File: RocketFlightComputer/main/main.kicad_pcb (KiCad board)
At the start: 4 copper layers, 53.7 x 53.7 mm, 127 parts, among them Q1 SI2302, Q2 SI2302, Q3 SI2302, Y1 32.768kHz, Y3 32.768kHz, Y4 32.768kHz, Y5 XRCGB24M000F2P29R0

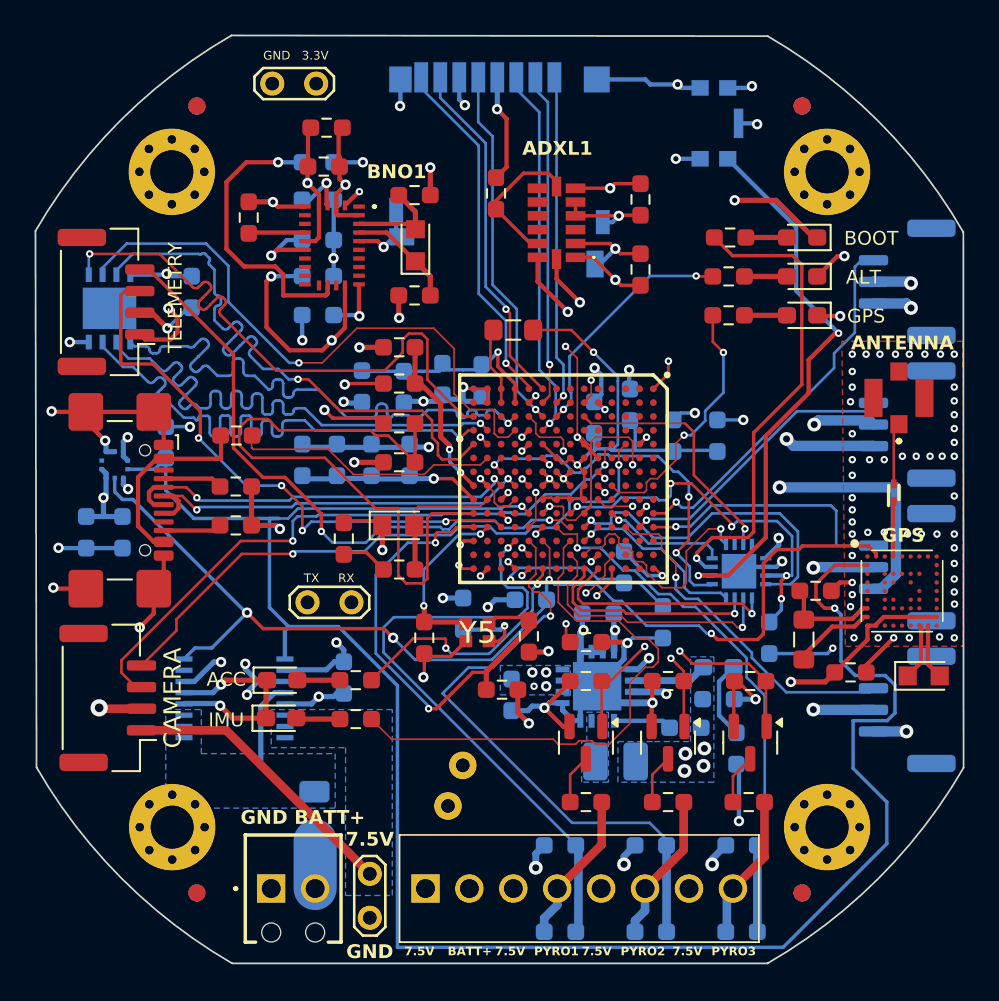
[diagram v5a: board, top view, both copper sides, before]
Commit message: Change of winbond flash to other one supported by teensy bootloader since winbond is out of stock
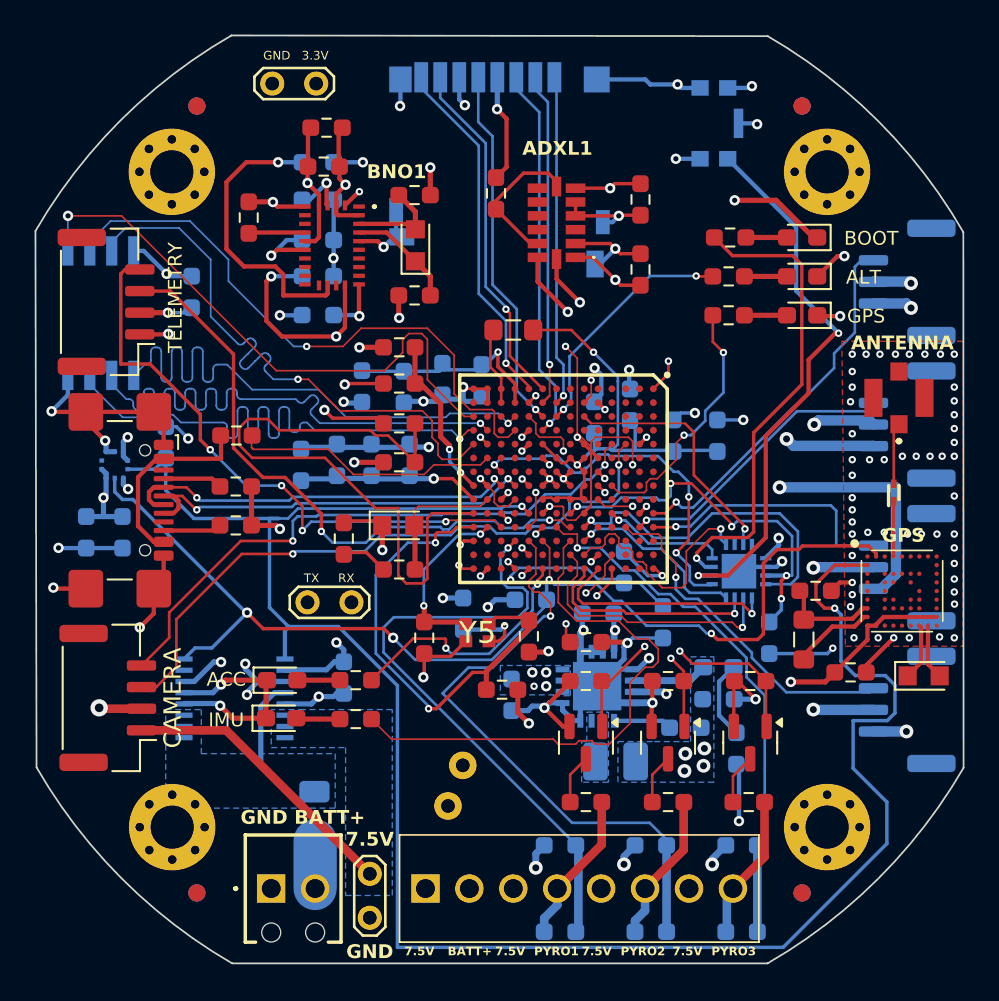
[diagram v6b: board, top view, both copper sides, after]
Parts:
- removed W25Q64JVXGIM_TR1: FLASH, footprint:SON80P400X400X50-9N
- added FLASH1: GD25Q64ESIG, footprint:GD25Q64ESIG, B.Cu at (86.8, 47.8)
- moved C6 0.30 mm to (98.4, 56.5)
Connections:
- MIMXRT1062DVL6B1 pad G11: /Xbee_RX -> /Xbee_TX
- MIMXRT1062DVL6B1 pad M11: /Xbee_TX -> /Xbee_RX
- S4B-PH-K-S_LF__SN_2 pad 3: /Cam_TX -> /Cam_RX
- S4B-PH-K-S_LF__SN_2 pad 4: /Cam_RX -> /Cam_TX
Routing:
- net GNDREF: track 255.0 -> 243.1 mm, vias 131 -> 130
- net /Cam_TX: track 37.5 -> 34.6 mm
- net +3.3V: track 111.2 -> 108.6 mm
- net /Xbee_TX: track 33.4 -> 35.9 mm, vias 4 -> 2
- net /Xbee_RX: track 36.4 -> 34.5 mm, vias 2 -> 4
- net /Cam_RX: track 35.9 -> 37.7 mm
- net /CS: track 33.3 -> 34.4 mm
- net Net-(MIMXRT1062DVL6B1-DCDC_IN_1): track 12.0 -> 11.0 mm
- net /BNO085_SCL: track 33.5 -> 32.8 mm
- net Net-(ADXL1-ADDR/SDO): track 8.37 -> 7.66 mm
- net /SD_B0_05: track 19.3 -> 18.6 mm
- net /CLK: track 34.8 -> 34.1 mm
- net /Servo4_PWM: track 21.8 -> 21.1 mm
- net /SD_B0_00: track 21.7 -> 21.0 mm
- net /SD_B0_03: track 20.6 -> 20.0 mm
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
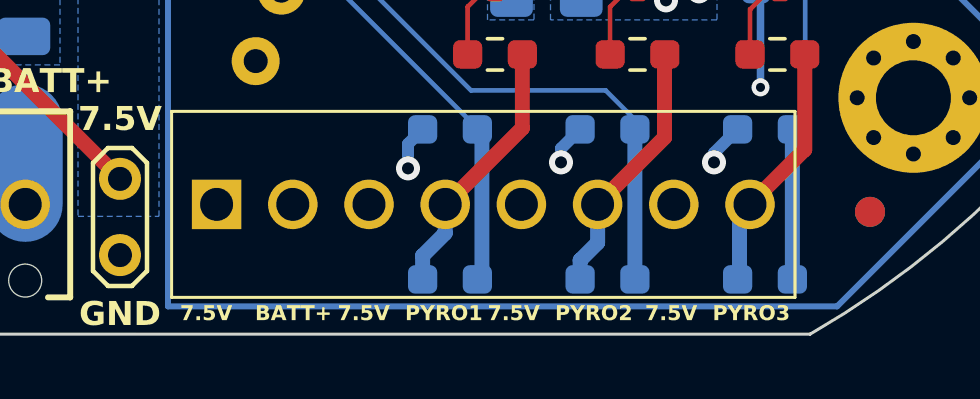
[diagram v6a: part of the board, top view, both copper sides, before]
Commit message: Final verification started, schematic verification of USBC and High current components
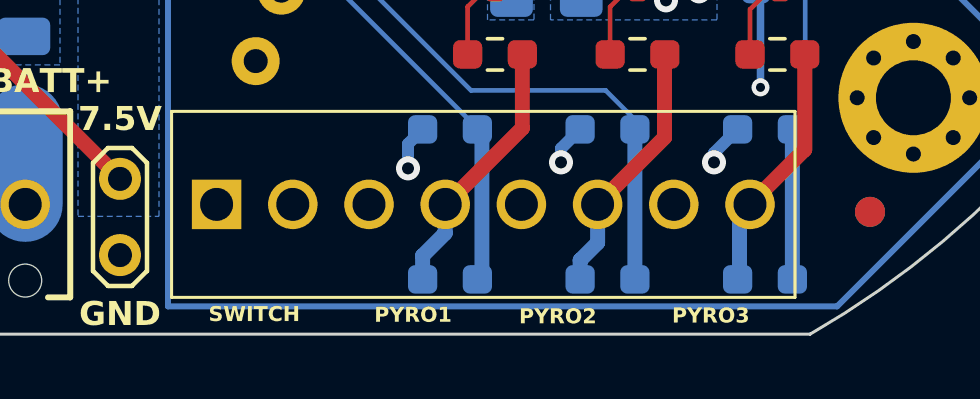
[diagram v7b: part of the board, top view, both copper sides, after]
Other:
- board text added: "SWITCH"
- board text removed: "BATT+"
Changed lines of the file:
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@@
 	)
 	(footprint "footprint:1725711"
-		(locked yes)
 		(layer "F.Cu")
 		(at 105.603 81.043)
@@
 		(layer "Edge.Cuts")
 	)
-	(gr_text "7.5V"
-		(locked yes)
-		(at 104.383 84.963 0)
-		(layer "F.SilkS")
-		(effects
-			(font
-				(size 0.5 0.5)
-				(thickness 0.08)
-				(bold yes)
-			)
-			(justify left bottom)
-		)
-	)
-	(gr_text "BATT+"
-		(locked yes)
-		(at 106.883 84.963 0)
-		(layer "F.SilkS")
-		(effects
-			(font
-				(size 0.5 0.5)
-				(thickness 0.08)
-				(bold yes)
-			)
-			(justify left bottom)
-		)
-	)
-	(gr_text "7.5V"
-		(locked yes)
-		(at 109.633 84.963 0)
+	(gr_text "SWITCH"
+		(at 105.333 84.993 0)
 		(layer "F.SilkS")
 		(effects
@@
 	)
 	(gr_text "PYRO1"
-		(locked yes)
-		(at 111.883 84.963 0)
-		(layer "F.SilkS")
-		(effects
-			(font
-				(size 0.5 0.5)
-				(thickness 0.08)
-				(bold yes)
-			)
-			(justify left bottom)
-		)
-	)
-	(gr_text "7.5V"
-		(locked yes)
-		(at 114.633 84.963 0)
+		(at 110.858 85.018 0)
 		(layer "F.SilkS")
 		(effects
@@
 	)
 	(gr_text "PYRO2"
-		(locked yes)
-		(at 116.883 84.963 0)
-		(layer "F.SilkS")
-		(effects
-			(font
-				(size 0.5 0.5)
-				(thickness 0.08)
-				(bold yes)
-			)
-			(justify left bottom)
-		)
-	)
-	(gr_text "7.5V"
-		(locked yes)
-		(at 119.883 84.963 0)
+		(at 115.683 85.068 0)
 		(layer "F.SilkS")
 		(effects
@@
 	)
 	(gr_text "PYRO3"
-		(locked yes)
-		(at 122.133 84.963 0)
+		(at 120.783 85.043 0)
 		(layer "F.SilkS")
 		(effects
@@
 		(layer "F.Cu")
 		(hatch none 0.1)
-		(priority 30003)
+		(priority 30004)
 		(attr
 			(teardrop
@@
 		(polygon
 			(pts
-				(xy 101.572211 79.028658) (xy 101.218658 79.382211) (xy 101.765655 80.522978) (xy 102.383707 80.193707)
-				(xy 102.712978 79.575655)
+				(xy 90.333 72.143) (xy 90.333 71.643) (xy 89.883 71.593) (xy 89.182 71.893) (xy 89.883 72.193)
 			)
 		)
@@
 		(layer "F.Cu")
 		(hatch none 0.1)
-		(priority 30004)
+		(priority 30003)
 		(attr
 			(teardrop
@@
 		(polygon
 			(pts
-				(xy 90.333 72.143) (xy 90.333 71.643) (xy 89.883 71.593) (xy 89.182 71.893) (xy 89.883 72.193)
+				(xy 101.572211 79.028658) (xy 101.218658 79.382211) (xy 101.765655 80.522978) (xy 102.383707 80.193707)
+				(xy 102.712978 79.575655)
 			)
 		)
@@
 	)
 	(zone
+		(net "/HighCurrentComponents/Pyro2_HighSide")
+		(layer "B.Cu")
+		(hatch none 0.1)
+		(priority 30008)
+		(attr
+			(teardrop
+				(type padvia)
+			)
+		)
+		(connect_pads yes
+			(clearance 0)
+		)
+		(min_thickness 0.0254)
+		(fill yes
+			(island_removal_mode 1)
+		)
+		(polygon
+			(pts
+				(xy 118.118247 82.861306) (xy 117.764694 82.507753) (xy 117.340581 83.112158) (xy 117.719793 83.543707)
+				(xy 118.189921 83.214613)
+			)
+		)
+	)
+	(zone
 		(net "+7.5V")
 		(layer "B.Cu")
@@
 	)
 	(zone
-		(net "/Pyro1_Test_40")
+		(net "/HighCurrentComponents/Pyro1_HighSide")
 		(layer "B.Cu")
 		(hatch none 0.1)
-		(priority 30005)
+		(priority 30007)
 		(attr
 			(teardrop
@@
 		(polygon
 			(pts
-				(xy 114.698 82.593) (xy 114.198 82.593) (xy 113.879852 83.136031) (xy 114.2955 83.544) (xy 114.783 83.3055)
+				(xy 112.762181 82.817371) (xy 112.408629 82.463819) (xy 112.040621 83.155431) (xy 112.469793 83.543707)
+				(xy 112.939921 83.214613)
 			)
 		)
 	)
 	(zone
-		(net "+3.3V")
+		(net "/Pyro2_Test_41")
 		(layer "B.Cu")
-		(hatch edge 0.5)
-		(priority 3)
+		(hatch none 0.1)
+		(priority 30004)
+		(attr
+			(teardrop
+				(type padvia)
+			)
+		)
 		(connect_pads yes
 			(clearance 0)
 		)
-		(min_thickness 0.25)
+		(min_thickness 0.0254)
 		(fill yes
-			(thermal_gap 0.5)
-			(thermal_bridge_width 0.5)
 			(island_removal_mode 1)
 		)
 		(polygon
 			(pts
-				(xy 122.283 67.643) (xy 122.283 74.893) (xy 116.733 74.893) (xy 116.733 72.543) (xy 118.833 72.543)
-				(xy 120.933 72.543) (xy 120.933 67.643)
+				(xy 119.7955 82.593) (xy 119.2955 82.593) (xy 119.076079 83.214613) (xy 119.5455 83.544) (xy 120.014921 83.214613)
 			)
 		)
 	)
 	(zone
-		(net "/HighCurrentComponents/Pyro3_HighSide")
+		(net "/Pyro1_Test_40")
 		(layer "B.Cu")
 		(hatch none 0.1)
-		(priority 30006)
+		(priority 30005)
 		(attr
 			(teardrop
@@
 		(polygon
 			(pts
-				(xy 123.283 82.593) (xy 122.783 82.593) (xy 122.517763 83.189642) (xy 122.9705 83.544) (xy 123.439921 83.214613)
+				(xy 114.698 82.593) (xy 114.198 82.593) (xy 113.879852 83.136031) (xy 114.2955 83.544) (xy 114.783 83.3055)
 			)
 		)
 	)
 	(zone
-		(net "+7.5V")
+		(net "/BMP390_SDA1")
 		(layer "B.Cu")
-		(hatch edge 0.5)
-		(priority 1)
+		(hatch none 0.1)
+		(priority 30010)
+		(attr
+			(teardrop
+				(type padvia)
+			)
+		)
 		(connect_pads yes
 			(clearance 0)
 		)
-		(min_thickness 0.25)
+		(min_thickness 0.0254)
 		(fill yes
-			(thermal_gap 0.5)
-			(thermal_bridge_width 0.5)
 			(island_removal_mode 1)
 		)
 		(polygon
 			(pts
-				(xy 113.983 68.143) (xy 109.933 68.143) (xy 109.933 69.843) (xy 113.033 69.843) (xy 113.033 69.893)
-				(xy 113.983 69.893)
+				(xy 91.971073 67.578548) (xy 91.829652 67.437127) (xy 91.577074 67.6156) (xy 91.639493 67.768707)
+				(xy 92.008126 67.615601)
 			)
 		)
@@
 	)
 	(zone
-		(net "+BATT")
+		(net "+3.3V")
 		(layer "B.Cu")
 		(hatch edge 0.5)
-		(priority 5)
+		(priority 3)
 		(connect_pads yes
 			(clearance 0)
@@
 			(thermal_gap 0.5)
 			(thermal_bridge_width 0.5)
-			(island_removal_mode 0)
-		)
-		(polygon
-			(pts
-				(xy 100.383 76.393) (xy 90.583 76.393) (xy 90.583 70.693) (xy 92.6406 70.693) (xy 92.6406 73.243)
-				(xy 100.383 73.243)
-			)
-		)
-	)
-	(zone
-		(net "/Pyro2_Test_41")
-		(layer "B.Cu")
-		(hatch none 0.1)
-		(priority 30004)
-		(attr
-			(teardrop
-				(type padvia)
-			)
-		)
-		(connect_pads yes
-			(clearance 0)
-		)
-		(min_thickness 0.0254)
-		(fill yes
 			(island_removal_mode 1)
 		)
 		(polygon
 			(pts
-				(xy 119.7955 82.593) (xy 119.2955 82.593) (xy 119.076079 83.214613) (xy 119.5455 83.544) (xy 120.014921 83.214613)
+				(xy 122.283 67.643) (xy 122.283 74.893) (xy 116.733 74.893) (xy 116.733 72.543) (xy 118.833 72.543)
+				(xy 120.933 72.543) (xy 120.933 67.643)
 			)
 		)
 	)
 	(zone
-		(net "/HighCurrentComponents/Pyro2_HighSide")
+		(net "+7.5V")
 		(layer "B.Cu")
-		(hatch none 0.1)
-		(priority 30008)
-		(attr
-			(teardrop
-				(type padvia)
-			)
-		)
+		(hatch edge 0.5)
+		(priority 1)
 		(connect_pads yes
 			(clearance 0)
 		)
-		(min_thickness 0.0254)
+		(min_thickness 0.25)
 		(fill yes
+			(thermal_gap 0.5)
+			(thermal_bridge_width 0.5)
 			(island_removal_mode 1)
 		)
 		(polygon
 			(pts
-				(xy 118.118247 82.861306) (xy 117.764694 82.507753) (xy 117.340581 83.112158) (xy 117.719793 83.543707)
-				(xy 118.189921 83.214613)
+				(xy 113.983 68.143) (xy 109.933 68.143) (xy 109.933 69.843) (xy 113.033 69.843) (xy 113.033 69.893)
+				(xy 113.983 69.893)
 			)
 		)
 	)
 	(zone
-		(net "/Pyro3_Test_39")
+		(net "/HighCurrentComponents/Pyro3_HighSide")
 		(layer "B.Cu")
 		(hatch none 0.1)
-		(priority 30003)
+		(priority 30006)
 		(attr
 			(teardrop
@@
 		(polygon
 			(pts
-				(xy 125.0455 82.593) (xy 124.5455 82.593) (xy 124.326079 83.214613) (xy 124.7955 83.544) (xy 125.264921 83.214613)
+				(xy 123.283 82.593) (xy 122.783 82.593) (xy 122.517763 83.189642) (xy 122.9705 83.544) (xy 123.439921 83.214613)
 			)
 		)
 	)
 	(zone
-		(net "/BMP390_SDA1")
+		(net "+BATT")
 		(layer "B.Cu")
-		(hatch none 0.1)
-		(priority 30010)
-		(attr
-			(teardrop
-				(type padvia)
-			)
-		)
+		(hatch edge 0.5)
+		(priority 5)
 		(connect_pads yes
 			(clearance 0)
 		)
-		(min_thickness 0.0254)
+		(min_thickness 0.25)
 		(fill yes
-			(island_removal_mode 1)
+			(thermal_gap 0.5)
+			(thermal_bridge_width 0.5)
+			(island_removal_mode 0)
 		)
 		(polygon
 			(pts
-				(xy 91.971073 67.578548) (xy 91.829652 67.437127) (xy 91.577074 67.6156) (xy 91.639493 67.768707)
-				(xy 92.008126 67.615601)
+				(xy 100.383 76.393) (xy 90.583 76.393) (xy 90.583 70.693) (xy 92.6406 70.693) (xy 92.6406 73.243)
+				(xy 100.383 73.243)
 			)
 		)
@@
 	)
 	(zone
-		(net "/HighCurrentComponents/Pyro1_HighSide")
+		(net "/Pyro3_Test_39")
 		(layer "B.Cu")
 		(hatch none 0.1)
-		(priority 30007)
+		(priority 30003)
 		(attr
 			(teardrop
@@
 		(polygon
 			(pts
-				(xy 112.762181 82.817371) (xy 112.408629 82.463819) (xy 112.040621 83.155431) (xy 112.469793 83.543707)
-				(xy 112.939921 83.214613)
+				(xy 125.0455 82.593) (xy 124.5455 82.593) (xy 124.326079 83.214613) (xy 124.7955 83.544) (xy 125.264921 83.214613)
 			)
 		)
@@
 	)
 	(zone
-		(net "/Reserve_TX")
+		(net "/Reserve_RX")
 		(layer "In2.Cu")
 		(hatch none 0.1)
-		(priority 30004)
+		(priority 30005)
 		(attr
 			(teardrop
@@
 		(polygon
 			(pts
-				(xy 99.715764 65.535366) (xy 99.825366 65.425764) (xy 99.452858 64.289801) (xy 98.782293 64.492293)
-				(xy 98.579801 65.162858)
+				(xy 102.365366 63.560236) (xy 102.255764 63.450634) (xy 101.119801 63.823142) (xy 101.322293 64.493707)
+				(xy 101.992858 64.696199)
 			)
 		)
@@
 	)
 	(zone
-		(net "/Reserve_RX")
+		(net "/Reserve_TX")
 		(layer "In2.Cu")
 		(hatch none 0.1)
-		(priority 30005)
+		(priority 30004)
 		(attr
 			(teardrop
@@
 		(polygon
 			(pts
-				(xy 102.365366 63.560236) (xy 102.255764 63.450634) (xy 101.119801 63.823142) (xy 101.322293 64.493707)
-				(xy 101.992858 64.696199)
+				(xy 99.715764 65.535366) (xy 99.825366 65.425764) (xy 99.452858 64.289801) (xy 98.782293 64.492293)
+				(xy 98.579801 65.162858)
 			)
 		)
@@
 		)
 	)
-	(group ""
-		(locked yes)
-		(members "0808fa44-a659-41c7-b718-3c499b156115" "10d50add-88a2-40ff-a374-7b5a79b52750"
-			"15cb6ab3-1305-4322-b703-005fcd8940ee" "a0f298d0-5286-476e-8946-1643024e492d"
-			"cae0bdb7-3dbd-44dd-8745-ee40b31359bc" "ce6a7408-7614-432f-8b24-932ff31c08cf"
-			"df7b5e33-0675-47ef-b6ad-99e23084827c" "e366ee4f-71de-49a1-b935-677bc3ad4a4a"
-			"e4e03c58-9230-49a6-a4a5-113e70bdc9e3"
-		)
-	)

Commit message: Corrected a few subsystems
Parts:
- removed C38: 4.7uF, Resistor_SMD:R_0603_1608Metric_Pad0.98x0.95mm_HandSolder
- removed D7: ESD9R3.3ST5G, footprint:ESD9R3_3ST5G
- removed L3: 2.2μH, Inductor_SMD:L_0805_2012Metric_Pad1.05x1.20mm_HandSolder
- removed R18: 10k, Resistor_SMD:R_0603_1608Metric_Pad0.98x0.95mm_HandSolder
- Q1: value SI2302 -> DMG3406L
- R22, R26: value 7k -> 10k
- R23, R27, R31: value 10k -> 7k
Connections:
- net /M1M2 renamed /SOC
- BNO1 pad 11: Net-(BNO1-NRST) -> /BNO085_RST
- CONMHF1-SMD-G-T1 pad 1: Net-(CONMHF1-SMD-G-T1-SIGNAL) -> /GPS ZOEM8/ANT
- MIMXRT1062DVL6B1 pad C3: unconnected-(MIMXRT1062DVL6B1-GPIO_EMC_36-PadC3) -> /BNO085_RST
- U-BLOX_ZOE_M8Q-0-1 pad 26: Net-(U-BLOX_ZOE_M8Q-0-1-V_DCDC_OUT) -> +3.3V
- U-BLOX_ZOE_M8Q-0-1 pad 27: Net-(U-BLOX_ZOE_M8Q-0-1-V_CORE) -> +3.3V
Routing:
- net /BNO085_RST: track 0.00 -> 43.2 mm
- net Net-(U-BLOX_ZOE_M8Q-0-1-V_CORE): track 5.32 -> 0.00 mm
- net Net-(U-BLOX_ZOE_M8Q-0-1-V_DCDC_OUT): track 4.59 -> 0.00 mm
- net Net-(BNO1-NRST): track 4.25 -> 0.00 mm, vias 1 -> 0
- net GNDREF: track 243.1 -> 238.9 mm, vias 130 -> 132
- net /GPS ZOEM8/ANT: track 3.18 -> 7.35 mm
- net Net-(CONMHF1-SMD-G-T1-SIGNAL): track 3.15 -> 0.00 mm
- net +3.3V: track 108.6 -> 109.6 mm
